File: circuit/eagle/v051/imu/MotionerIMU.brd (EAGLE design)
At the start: 41.9 x 33 mm, 53 parts, among them J1 AVR ISP, U1 ATMEGA328, U2 5V, U3 3.3V, U4 MPU-6050-1, U5 HMC5883L, U6 MCP2515, U7 MCP2551, Y1 16MHz, Y2 16MHz

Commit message: Load free node structure from XML file
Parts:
- moved JP5 24.3 mm to (36.2, 27.3)
- moved JP2 23.8 mm to (5.71, 5.71)
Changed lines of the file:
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@@
 <layer number="45" name="Holes" color="7" fill="1" visible="no" active="yes"/>
 <layer number="46" name="Milling" color="3" fill="1" visible="no" active="yes"/>
-<layer number="47" name="Measures" color="7" fill="1" visible="no" active="yes"/>
+<layer number="47" name="Measures" color="7" fill="1" visible="yes" active="yes"/>
 <layer number="48" name="Document" color="7" fill="1" visible="yes" active="yes"/>
 <layer number="49" name="Reference" color="7" fill="1" visible="yes" active="yes"/>
@@
 <element name="JP3" library="SparkFun" package="STAND-OFF-TIGHT" value="STAND-OFFTIGHT" x="39.37" y="30.48" rot="R180"/>
 <element name="JP4" library="SparkFun" package="STAND-OFF-TIGHT" value="STAND-OFFTIGHT" x="2.54" y="2.54" rot="R180"/>
-<element name="JP2" library="SparkFun" package="MICRO-FIDUCIAL" value="FIDUCIALUFIDUCIAL" x="1.905" y="29.21" rot="R180"/>
-<element name="JP5" library="SparkFun" package="MICRO-FIDUCIAL" value="FIDUCIALUFIDUCIAL" x="39.37" y="3.175" rot="R180"/>
+<element name="JP2" library="SparkFun" package="MICRO-FIDUCIAL" value="FIDUCIALUFIDUCIAL" x="5.715" y="5.715" rot="R180"/>
+<element name="JP5" library="SparkFun" package="MICRO-FIDUCIAL" value="FIDUCIALUFIDUCIAL" x="36.195" y="27.305" rot="R180"/>
 <element name="U$2" library="SparkFun-Aesthetics" package="OSHW-LOGO-S" value="OSHW-LOGOS" x="38.1" y="3.302" rot="MR0"/>
 <element name="U2" library="SparkFun" package="SOT23-5" value="5V" x="11.43" y="6.985" smashed="yes" rot="R90">

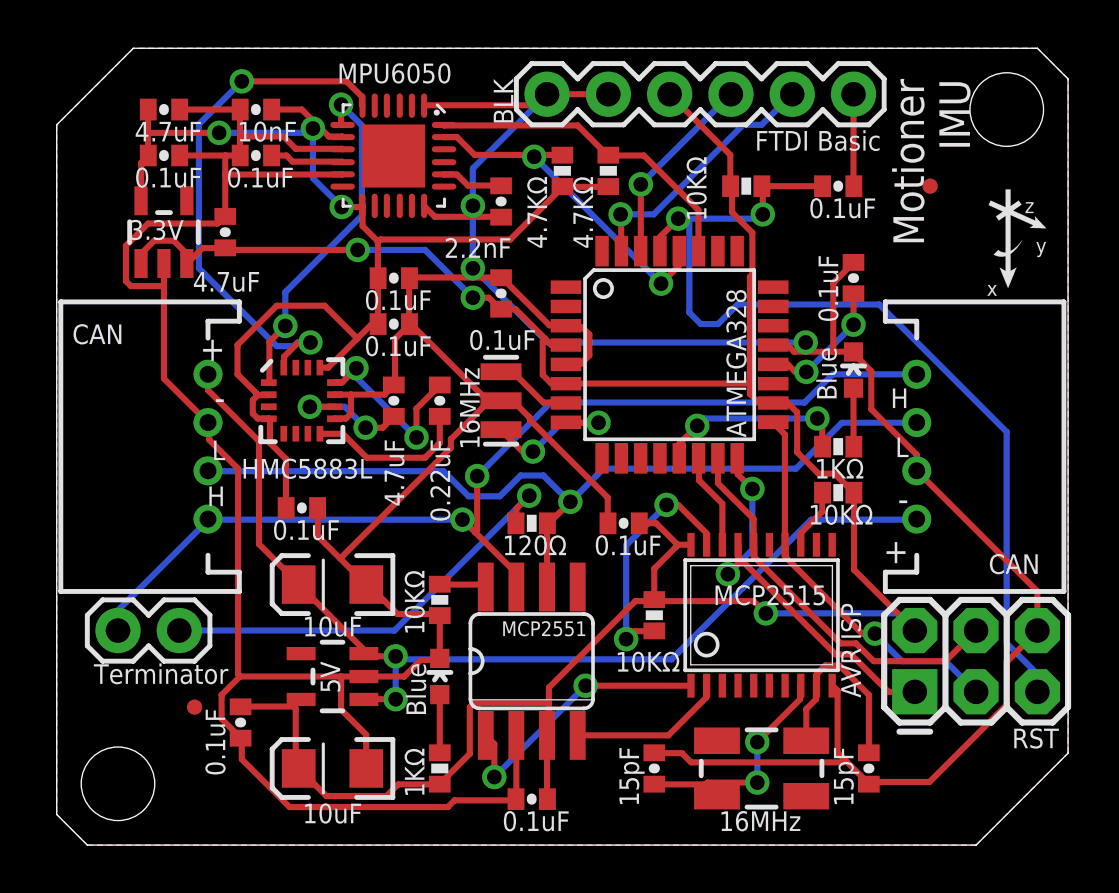
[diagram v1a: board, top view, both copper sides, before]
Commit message: made longer soldering pads for the HMC5883L
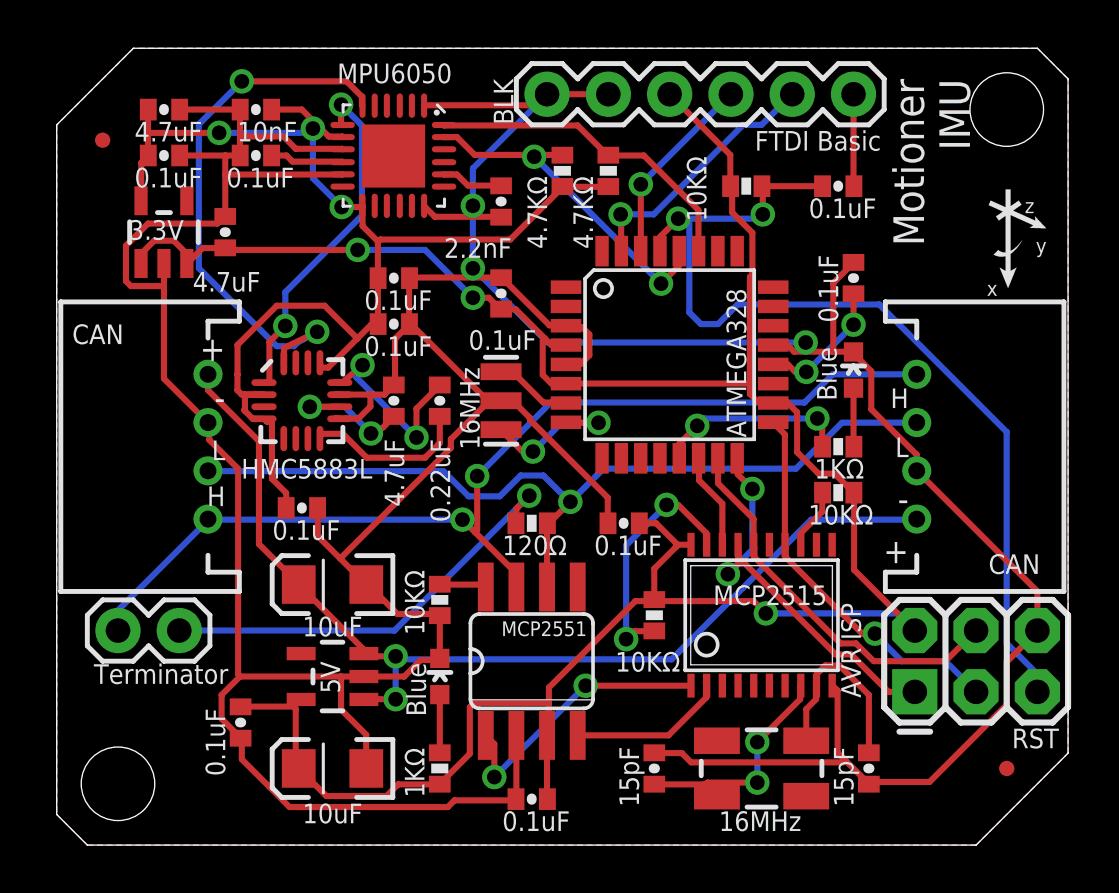
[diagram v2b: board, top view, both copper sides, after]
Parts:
- moved JP5 24.3 mm to (39.4, 3.17)
- moved JP2 23.8 mm to (1.91, 29.2)
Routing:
- net 3.3V: track 52.7 -> 54.0 mm
- net XDA: track 21.9 -> 23.1 mm
- net GND: track 209.2 -> 210.2 mm
- net N$5: track 7.62 -> 8.26 mm
